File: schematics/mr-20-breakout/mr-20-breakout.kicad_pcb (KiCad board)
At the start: 2 copper layers, 90 x 75 mm, 10 parts, among them CN1 MR-50RMA+, J1 PTSA-1.5-10-3.5-Z, J2 PTSA-1.5-10-3.5-Z, J3 PTSA-1.5-10-3.5-Z, J4 PTSA-1.5-10-3.5-Z, J5 PTSA-1.5-10-3.5-Z

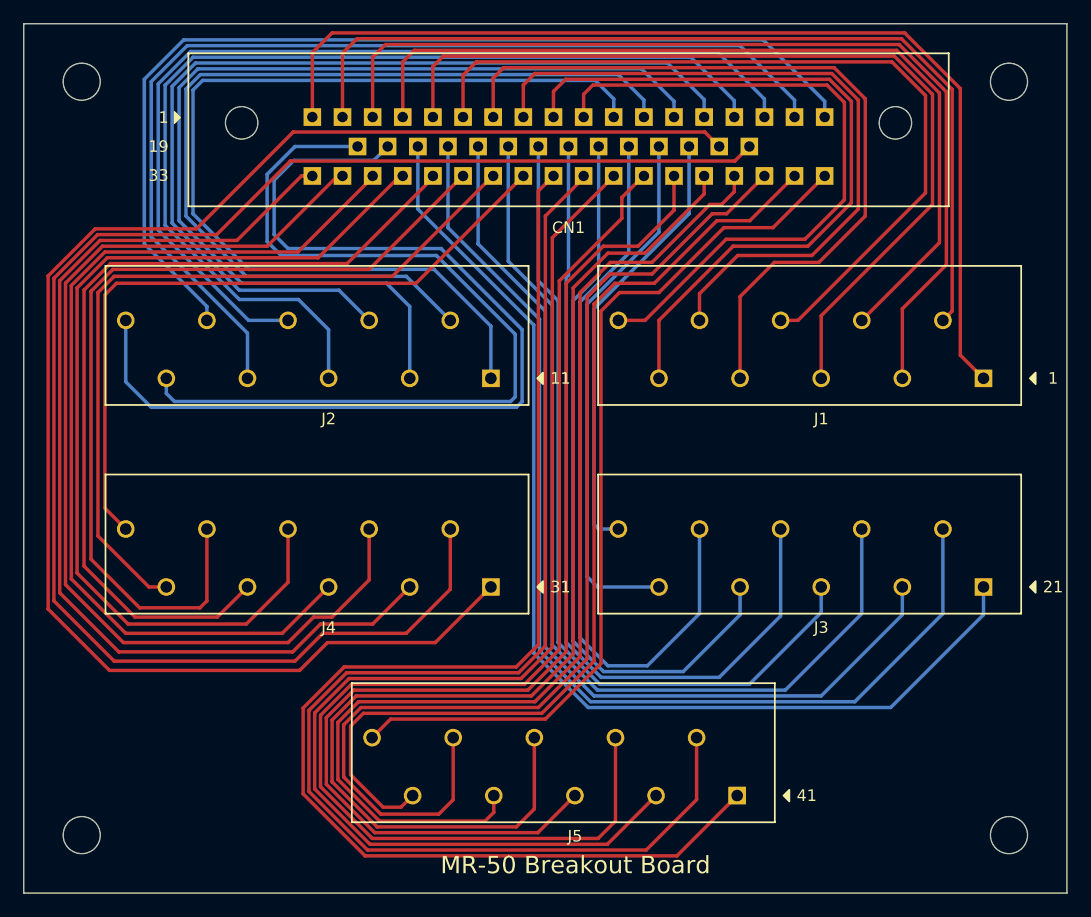
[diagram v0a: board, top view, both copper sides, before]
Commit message: Added MR-20 breakout board schematics
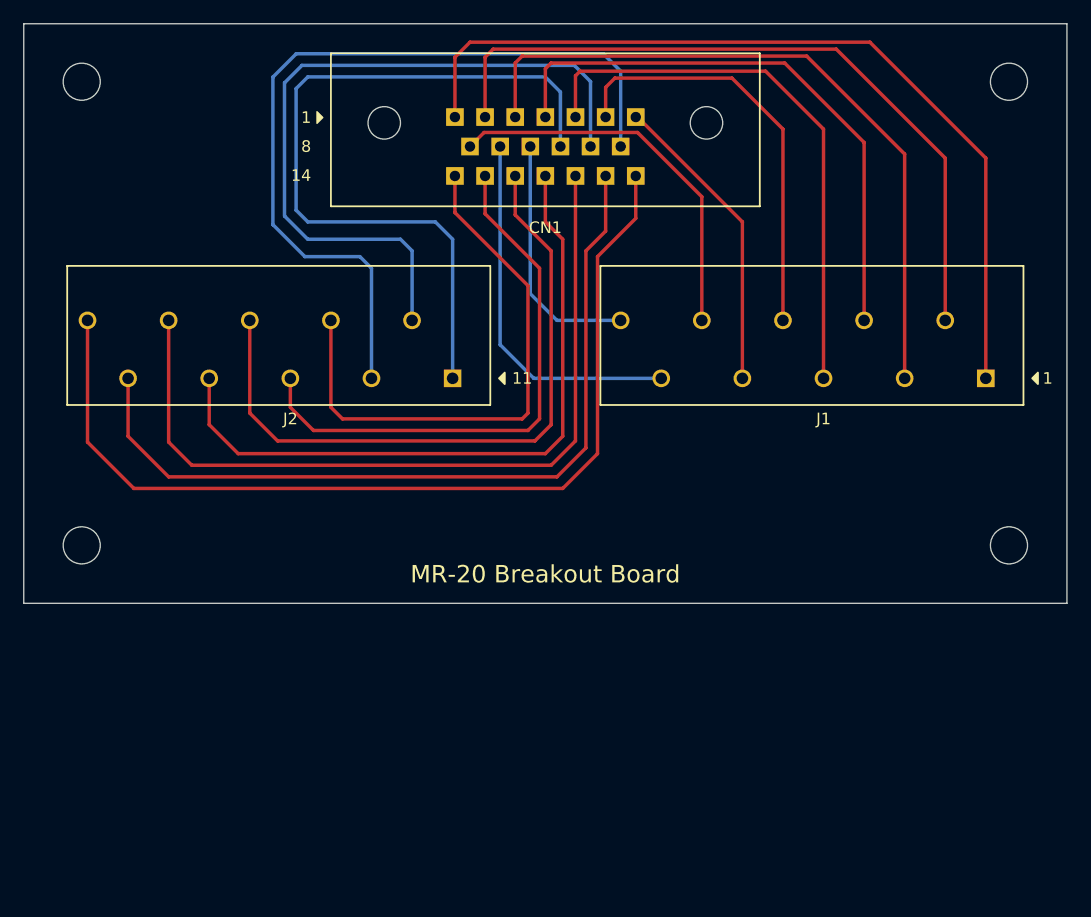
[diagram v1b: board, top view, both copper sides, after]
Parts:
- removed J3, J4, J5: PTSA-1.5-10-3.5-Z, Connector_Phoenix_PTSA:PhoenixContact_PTSA_1,5_10_3,5-Z
- CN1: value MR-50RMA+ -> MR-20RMA+; footprint Connector_Honda:MR-50RMA+ -> Connector_Honda:MR-20RMA+
- moved REF** 25.0 mm to (188.0, 64.4)
- moved REF** 25.0 mm to (108.0, 64.4)
- moved J2 3.30 mm to (140.0, 50.0)
- moved CN1 2.00 mm to (148.0, 30.0)
- moved J1 0.20 mm to (186.0, 50.0)
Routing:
- net Net-(CN1-Pad32): track 136.7 -> 0.00 mm
- net Net-(CN1-Pad31): track 135.7 -> 0.00 mm
- net Net-(CN1-Pad42): track 114.3 -> 0.00 mm
- net Net-(CN1-Pad41): track 112.8 -> 0.00 mm
- net Net-(CN1-Pad44): track 108.1 -> 0.00 mm
- net Net-(CN1-Pad43): track 105.4 -> 0.00 mm
- net Net-(CN1-Pad46): track 102.2 -> 0.00 mm
- net Net-(CN1-Pad45): track 100.0 -> 0.00 mm
- net Net-(CN1-Pad48): track 95.3 -> 0.00 mm
- net Net-(CN1-Pad47): track 94.5 -> 0.00 mm
- net Net-(CN1-Pad21): track 94.3 -> 0.00 mm
- net Net-(CN1-Pad22): track 93.8 -> 0.00 mm
- net Net-(CN1-Pad34): track 88.7 -> 0.00 mm
- net Net-(CN1-Pad49): track 87.1 -> 0.00 mm
- net Net-(CN1-Pad33): track 87.1 -> 0.00 mm
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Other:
- board size 90 x 75 mm -> 90 x 50 mm
- board text added: "MR-20 Breakout Board"
- board text removed: "MR-50 Breakout Board"
